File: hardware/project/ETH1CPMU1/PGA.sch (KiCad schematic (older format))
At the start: 47 parts, among them Q1401 BC847, Q1402 BC847, Q1403 BC847, Q1404 BC847, Q1405 BC847, Q1406 BC847, U1401 PGA103, U1402 PGA103, U1403 PGA103, U1404 OPA602, U1405 OPA602

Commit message: PCB design
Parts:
- added C1418, C1419: 100n, Capacitor_SMD:C_0603_1608Metric_Pad1.05x0.95mm_HandSolder, symbol Device:C
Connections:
- net +15VF: now also C1418.1
- net -15VF: now also C1419.1
- net AGNDF: now also C1418.2, C1419.2
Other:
- moved on the sheet: C1404, C1405, C1406, C1407, C1408, C1409, C1416, C1417

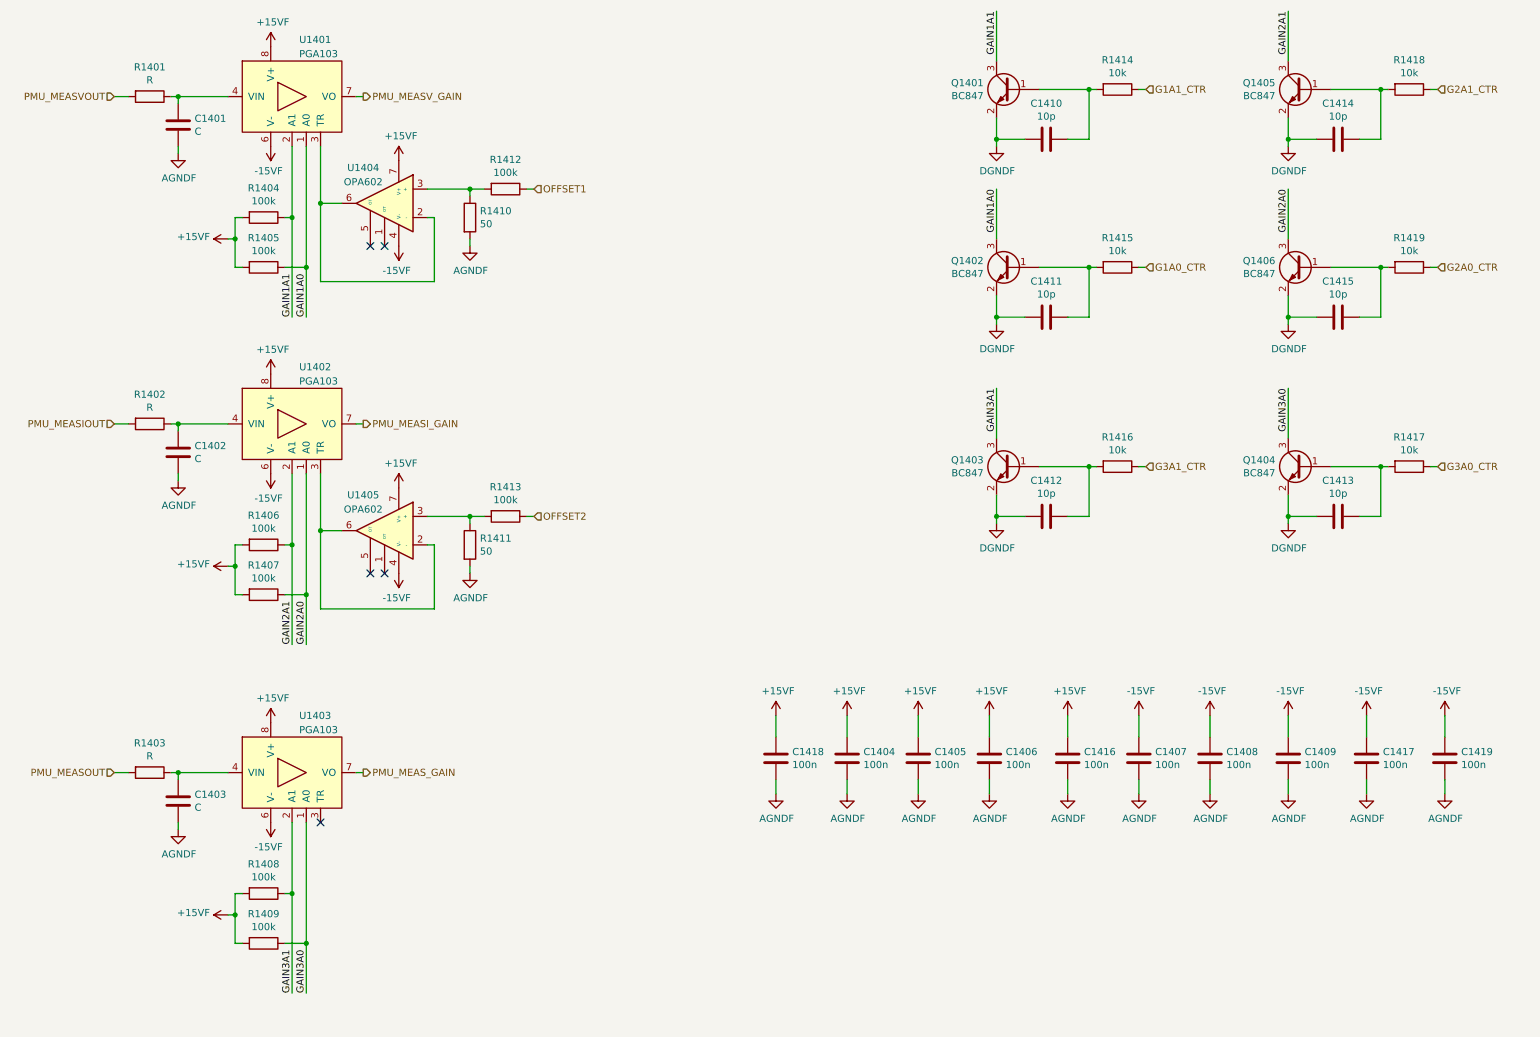
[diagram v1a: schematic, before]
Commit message: Added two analog switches
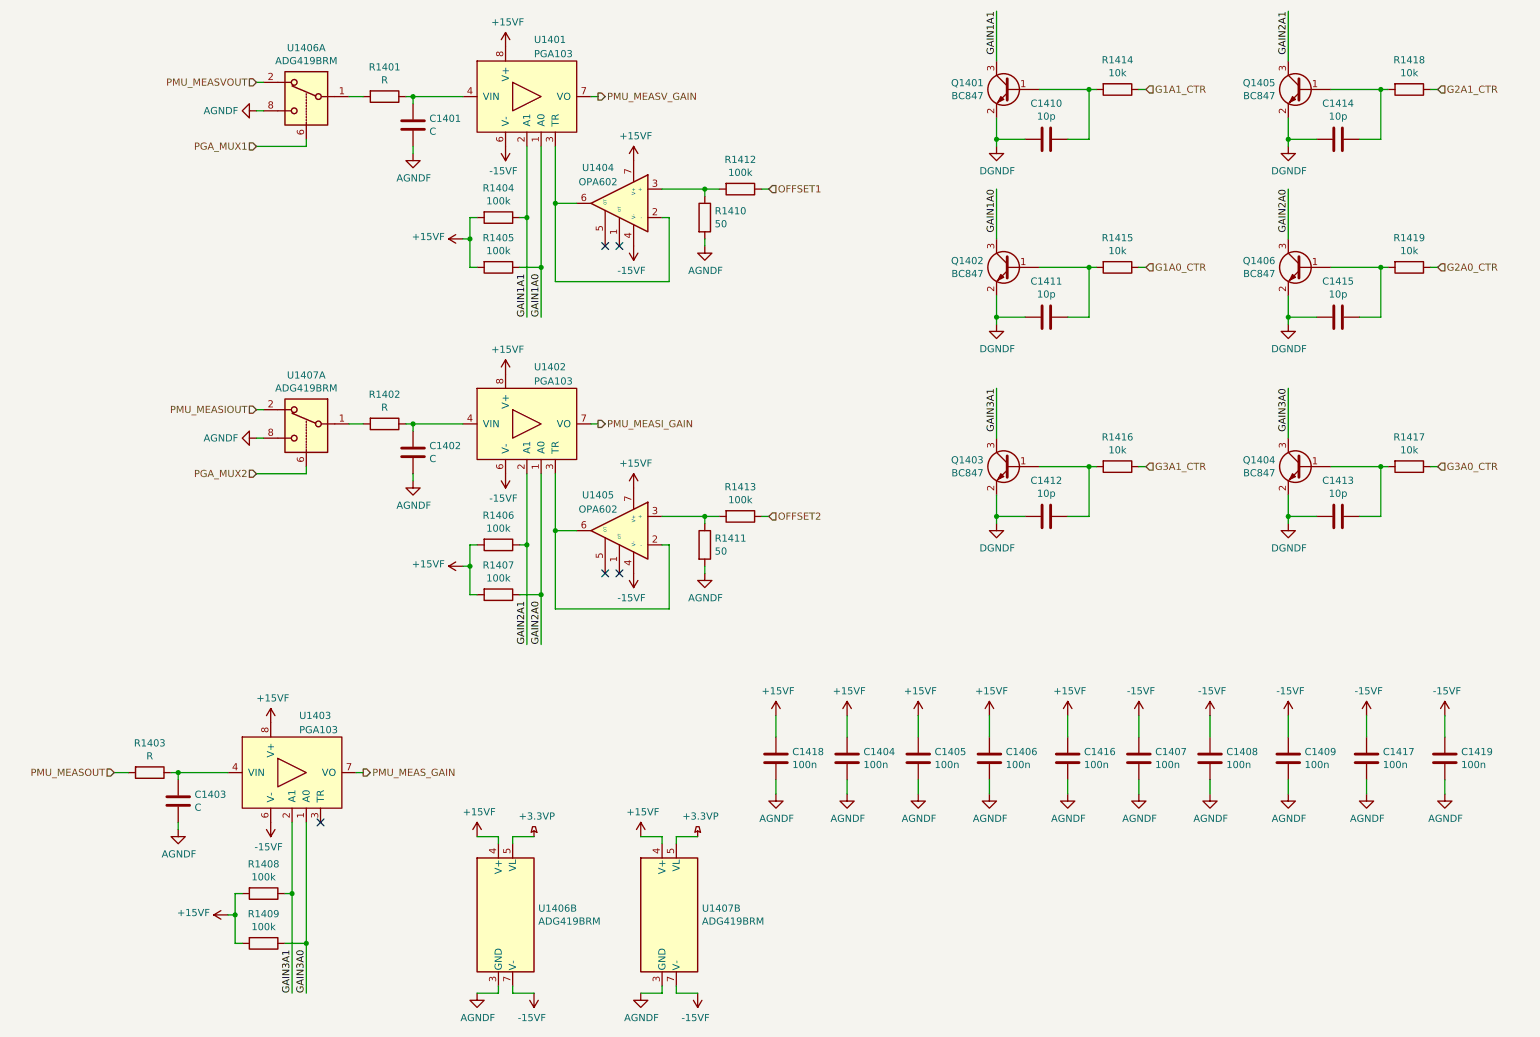
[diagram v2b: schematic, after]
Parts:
- added U1406, U1407: ADG419BRM, Package_SO:MSOP-8_3x3mm_P0.65mm, symbol Analog_Switch:ADG419BRM
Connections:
- net +15VF: now also U1406.4 (V+), U1407.4 (V+)
- net -15VF: now also U1406.7 (V-), U1407.7 (V-)
- net AGNDF: now also U1406.3 (GND), U1406.8, U1407.3 (GND), U1407.8
- net PMU_MEASIOUT: now also U1407.2; no longer R1402.2
- net PMU_MEASVOUT: now also U1406.2; no longer R1401.2
- new net: R1401.2, U1406.1
- new net: R1402.2, U1407.1
- new net +3.3VP: U1406.5 (VL), U1407.5 (VL)
- new net PGA_MUX1: U1406.6
- new net PGA_MUX2: U1407.6
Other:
- moved on the sheet: C1401, C1402, R1401, R1402, R1404, R1405, R1406, R1407, R1410, R1411, R1412, R1413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
